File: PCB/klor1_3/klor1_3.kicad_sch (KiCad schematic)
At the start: 88 parts, among them J1 MJ-4PP-9, J2 Haptic Buzz, J3 lv27, SW1 SW_PUSH-MX_W_LED, SW10 SW_PUSH-MX_W_LED, SW11 SW_PUSH-MX_W_LED, SW12 SW_PUSH-MX_W_LED, SW13 SW_PUSH-MX_W_LED, SW14 SW_PUSH-MX_W_LED, SW15 SW_PUSH-MX_W_LED, SW16 SW_PUSH-MX_W_LED, SW17 SW_PUSH-MX_W_LED, SW18 RotaryEncoder_Switch, SW19 SW_PUSH-MX_W_LED, SW2 SW_PUSH-MX_W_LED, SW20 SW_PUSH-MX_W_LED, SW21 SW_PUSH-MX_W_LED, SW22 SW_PUSH-MX_W_LED, SW3 SW_PUSH-MX_W_LED, SW4 SW_PUSH-MX_W_LED, SW5 SW_PUSH-MX_W_LED, SW6 SW_PUSH-MX_W_LED, SW7 SW_PUSH-MX_W_LED, SW8 SW_PUSH-MX_W_LED, SW9 SW_PUSH-MX_W_LED, U1 ProMicro

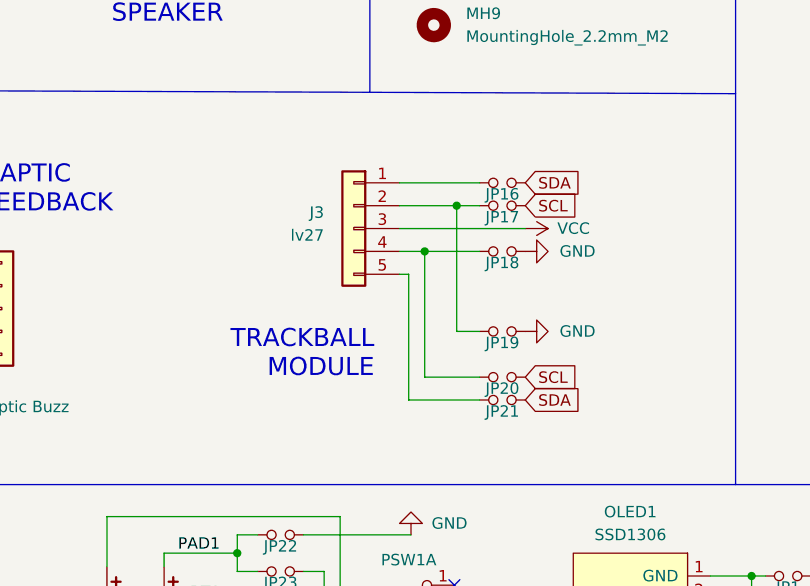
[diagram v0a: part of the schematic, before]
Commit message: modified KLOR to use KS-27 switches, and no longer supports the trackball
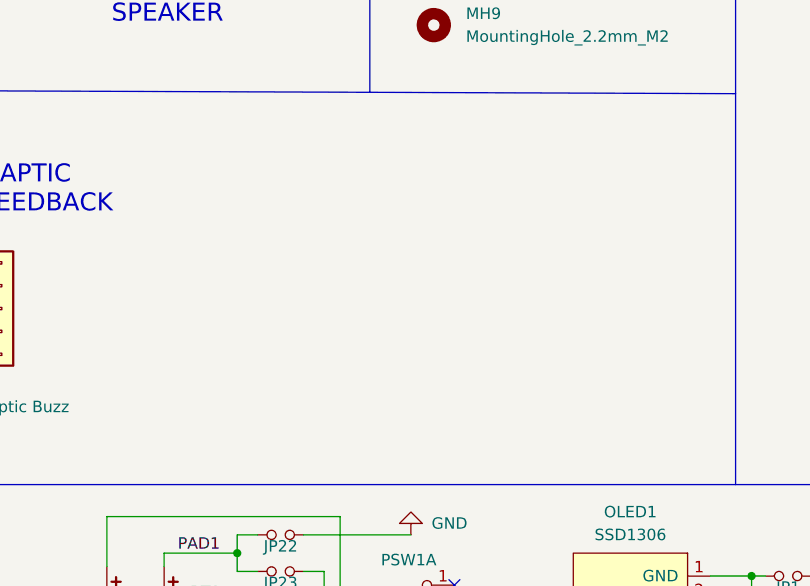
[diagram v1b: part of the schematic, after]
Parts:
- removed J3: lv27, KLOR:lvc27_onlyInput, symbol Connector_Generic:Conn_01x05
- removed JP16, JP17, JP18, JP19, JP21: Device_Jumper_NO_Small, KLOR:Jumper, symbol KLORlib:Device_Jumper_NO_Small
- removed JP20: Device_Jumper_NO_Small, KLOR:Jumper, symbol SofleKeyboard-cache:Device_Jumper_NO_Small
- SW1, SW10, SW11, SW12, SW13, SW14, SW15, SW16, SW17, SW19, SW2, SW20, SW21, SW22, SW3, SW4, SW5, SW6, SW7, SW8, SW9: footprint KLOR:SK6812MINI_and_cherry -> fingerpunch:gateron-ks27-reversible-with-sk6812-mini-e
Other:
- note removed: "TRACKBALL MODULE"
